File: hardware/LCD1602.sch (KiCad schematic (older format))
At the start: 6 parts, among them U2 RC1602A, U3 TXB0108PWR

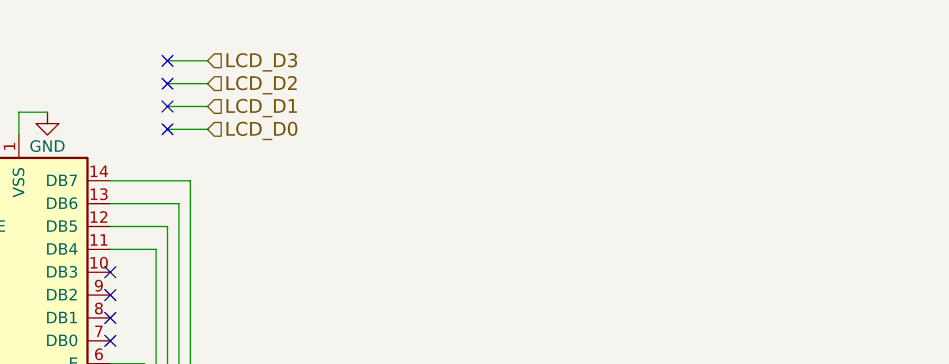
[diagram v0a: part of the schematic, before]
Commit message: Finished work on Receiver RPi shield. Changed CLK to SI5351A. Minimized footprints for almost all Tayloe detector ICs. Added -12V to audio opamps. Prepared board for coexisting with Hifiberry.
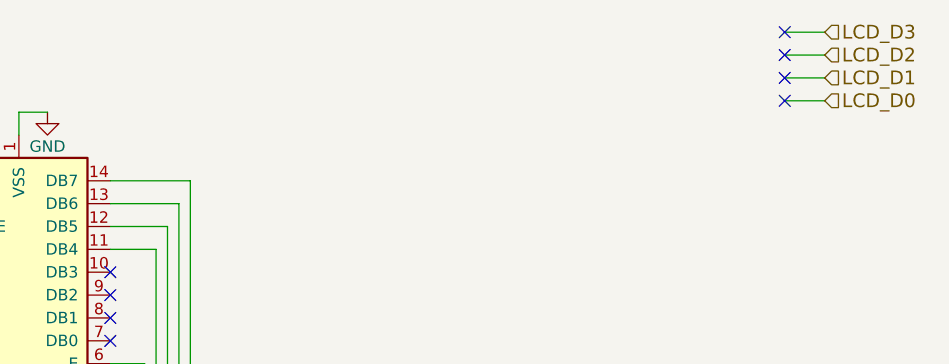
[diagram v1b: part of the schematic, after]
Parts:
- U2: footprint Connector_PinHeader_2.54mm:PinHeader_1x16_P2.54mm_Vertical -> Connector_FFC-FPC:Hirose_FH12-16S-0.5SH_1x16-1MP_P0.50mm_Horizontal
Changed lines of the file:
@@
 EESchema Schematic File Version 4
 LIBS:rf-receiver-cache
-EELAYER 26 0
+EELAYER 29 0
 EELAYER END
 $Descr A4 11693 8268
@@
 Text HLabel 4900 5200 0    60   Input ~ 0
 LCD_EN
-Text HLabel 6100 2775 2    60   Input ~ 0
+Text HLabel 8800 2650 2    60   Input ~ 0
 LCD_D0
-Text HLabel 6100 2675 2    60   Input ~ 0
+Text HLabel 8800 2550 2    60   Input ~ 0
 LCD_D1
-Text HLabel 6100 2575 2    60   Input ~ 0
+Text HLabel 8800 2450 2    60   Input ~ 0
 LCD_D2
-Text HLabel 6100 2475 2    60   Input ~ 0
+Text HLabel 8800 2350 2    60   Input ~ 0
 LCD_D3
 Text HLabel 4900 5300 0    60   Input ~ 0
@@
 NoConn ~ 5675 3700
 Wire Wire Line
-	6100 2475 5925 2475
+	8800 2350 8625 2350
 Wire Wire Line
-	6100 2575 5925 2575
+	8800 2450 8625 2450
 Wire Wire Line
-	6100 2675 5925 2675
+	8800 2550 8625 2550
 Wire Wire Line
-	6100 2775 5925 2775
-NoConn ~ 5925 2475
-NoConn ~ 5925 2575
-NoConn ~ 5925 2675
-NoConn ~ 5925 2775
+	8800 2650 8625 2650
+NoConn ~ 8625 2350
+NoConn ~ 8625 2450
+NoConn ~ 8625 2550
+NoConn ~ 8625 2650
 $Comp
 L athir:RC1602A U2
@@
 F 0 "U2" H 5025 4150 50  0000 C CNN
 F 1 "RC1602A" H 5385 4150 50  0000 L CNN
-F 2 "Connector_PinHeader_2.54mm:PinHeader_1x16_P2.54mm_Vertical" H 5375 2700 50  0001 C CNN
+F 2 "Connector_FFC-FPC:Hirose_FH12-16S-0.5SH_1x16-1MP_P0.50mm_Horizontal" H 5375 2700 50  0001 C CNN
 F 3 "" H 5375 3400 50  0001 C CNN
 	1    5275 3500
